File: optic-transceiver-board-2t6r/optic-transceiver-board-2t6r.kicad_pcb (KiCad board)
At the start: 2 copper layers, 38.8 x 63.7 mm, 49 parts, among them J1 Conn_02x08_Odd_Even, U1 HFBR-1521Z, U2 HFBR-2521Z, U3 HFBR-2521Z, U4 HFBR-2521Z, U5 HFBR-2521Z, U6 HFBR-2521Z, U7 HFBR-2521Z, U8 HFBR-1521Z, U9 74HCT541

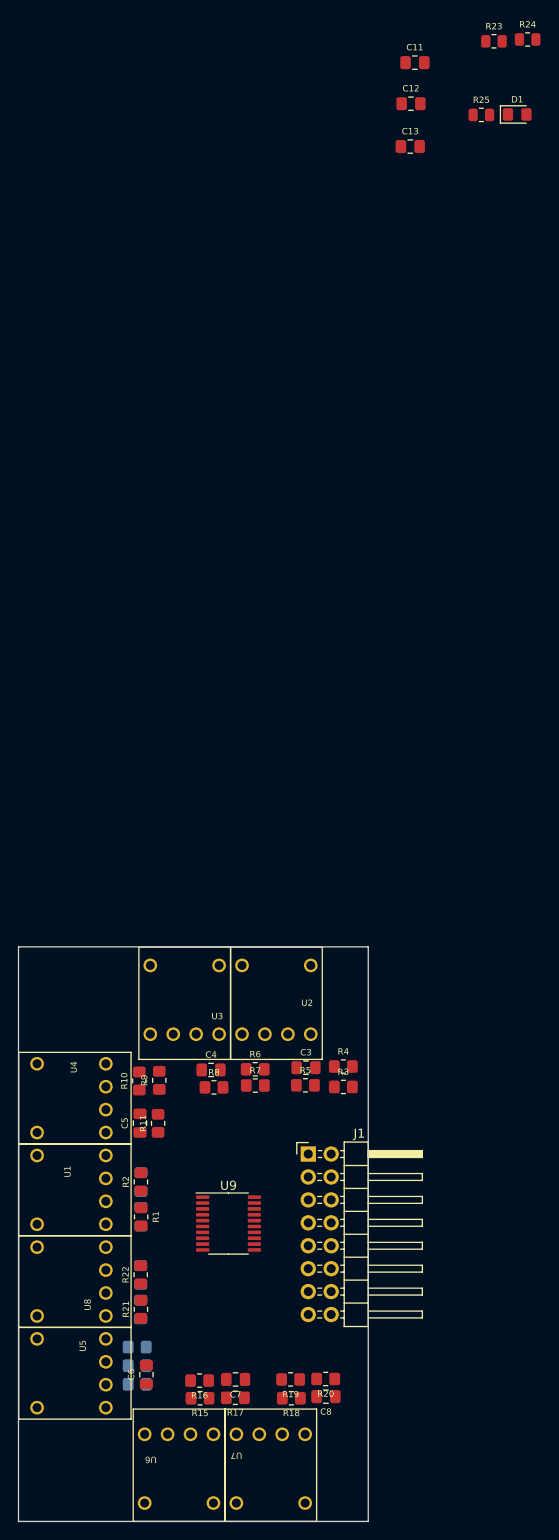
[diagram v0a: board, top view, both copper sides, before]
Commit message: Finalized optic boards, modified sil in adc-fiber interface board
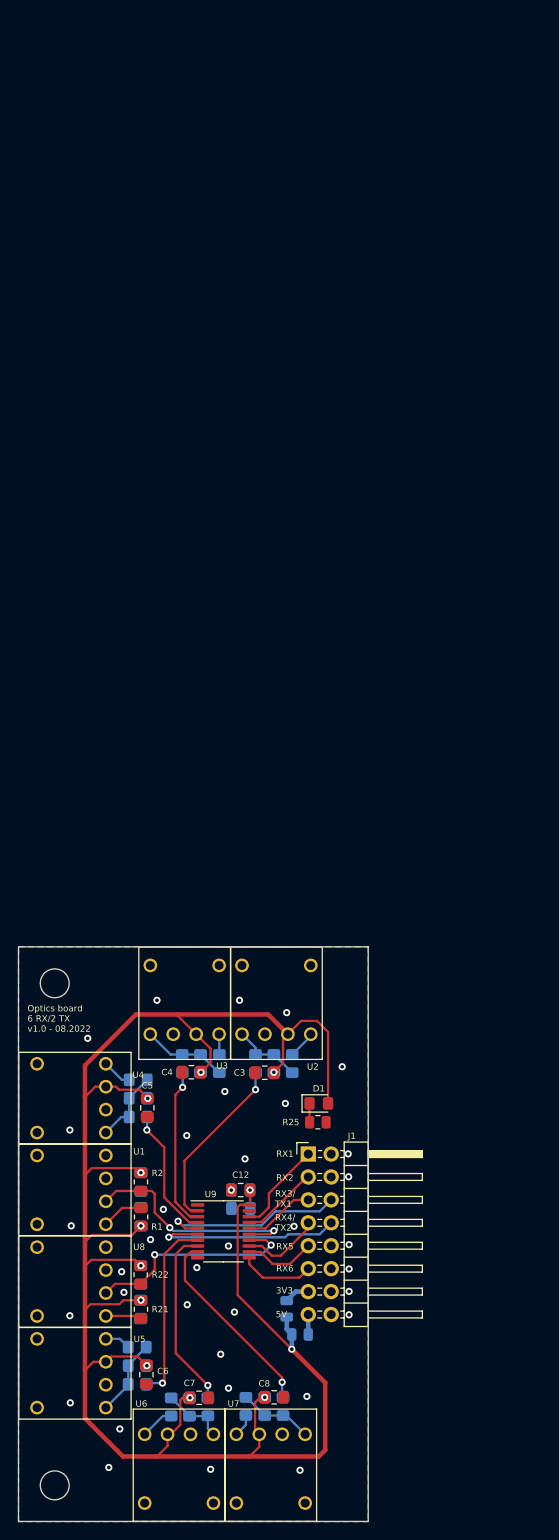
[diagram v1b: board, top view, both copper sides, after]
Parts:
- added REF**: MountingHole_3.2mm_M3, MountingHole:MountingHole_3.2mm_M3, F.Cu at (86.7, 47.0)
- added REF**: MountingHole_3.2mm_M3, MountingHole:MountingHole_3.2mm_M3, F.Cu at (86.7, 102.7)
- C11, C13, R10, R11, R15, R16, R17, R18, R19, R20, R23, R24, R3, R4, R5, R6, R7, R8, R9: moved to B.Cu
- moved R23 144.9 mm to (113.9, 86.0)
- moved R24 143.2 mm to (112.4, 83.1), turned to 90 degrees
- moved C11 126.4 mm to (107.3, 70.0)
- moved C12 121.8 mm to (107.3, 70.0)
- moved C13 119.1 mm to (107.3, 72.0)
- moved R25 113.1 mm to (115.9, 62.4)
- moved D1 111.8 mm to (116.0, 60.4)
- moved R4 7.70 mm to (111.0, 55.9), turned to -90 degrees
- moved R7 6.54 mm to (102.9, 55.9), turned to -90 degrees
- moved R3 6.22 mm to (113.0, 55.9), turned to 90 degrees
- moved R5 6.03 mm to (109.0, 55.9), turned to 90 degrees
- moved C8 5.74 mm to (111.0, 92.9)
- moved R20 5.62 mm to (112.0, 93.9), turned to -90 degrees
- moved R18 5.12 mm to (107.9, 93.9), turned to -90 degrees
- moved C3 4.61 mm to (110.0, 56.9)
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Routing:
- net VCC: track 0.00 -> 219.8 mm, vias 0 -> 12
- net /TX1b: track 0.00 -> 25.0 mm, vias 0 -> 2
- net /TX2b: track 0.00 -> 24.1 mm, vias 0 -> 2
- net /TX2: track 0.00 -> 22.0 mm, vias 0 -> 1
- net /RX6: track 0.00 -> 21.7 mm, vias 0 -> 1
- net /TX1: track 0.00 -> 20.8 mm, vias 0 -> 1
- net /RX4: track 0.00 -> 20.5 mm, vias 0 -> 1
- net /RX5: track 0.00 -> 20.2 mm, vias 0 -> 1
- net /RX1: track 0.00 -> 19.6 mm, vias 0 -> 1
- net /RX2: track 0.00 -> 17.8 mm, vias 0 -> 1
- net /RX3: track 0.00 -> 14.6 mm, vias 0 -> 1
- net /RX1b: track 0.00 -> 10.3 mm
- net Net-(R6-Pad1): track 0.00 -> 9.41 mm
- net /RX4b: track 0.00 -> 8.83 mm
- net /RX2b: track 0.00 -> 8.63 mm
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- added copper zone on B.Cu, net GND
- added copper zone on F.Cu, net GND
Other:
- board text added: "3V3"
- board text added: "5V"
- board text added: "Optics board 6 RX/2 TX v1.0 - 08.2022"
- board text added: "RX1"
- board text added: "RX2"
- board text added: "RX3/ TX1"
- board text added: "RX4/ TX2"
- board text added: "RX5"
- board text added: "RX6"

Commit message: Generated gerber files for optic-transceiver board
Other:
- board text added: "RX3"
- board text added: "RX4"
- board text added: "TX1"
- board text added: "TX2"
